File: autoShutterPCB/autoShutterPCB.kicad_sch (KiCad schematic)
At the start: 0 parts

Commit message: feat: Finish pcb, going to check how much it would cost
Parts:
- added Button1: SW_Push, Button_Switch_THT:SW_PUSH_6mm, symbol Switch:SW_Push
- added OLED1: Conn_01x04_Socket, Connector:FanPinHeader_1x04_P2.54mm_Vertical, symbol Connector:Conn_01x04_Socket
- added R1, R2, R3, R4: R, Resistor_THT:R_Axial_DIN0207_L6.3mm_D2.5mm_P10.16mm_Horizontal, symbol Device:R
- added TRS1: Conn_01x04_Socket, Audio_Module:TRS_SMD, symbol Connector:Conn_01x04_Socket
- added Transistor(Ring)1, Transistor(Tip)1: MMBT2222A, Package_TO_SOT_SMD:SOT-23, symbol Transistor_BJT:MMBT2222A
- added U1: XIAO-RP2040-DIP, Xiao RP2040:XIAO-RP2040-DIP, symbol Xiao RP2040:XIAO-RP2040-DIP
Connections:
- new net: R2.2, R3.1, Transistor(Ring)1.1 (B)
- new net: R1.2, R4.1, Transistor(Tip)1.1 (B)
- new net +3V3: OLED1.3 (Pin_3)
- new net GND: Button1.1, OLED1.4 (Pin_4), R3.2, R4.2, TRS1.2 (Pin_2), Transistor(Ring)1.2 (E), Transistor(Tip)1.2 (E), U1.13 (GND)
- new net d0: R1.1, U1.1 (P26_A0_D0)
- new net d1: R2.1, U1.2 (P27_A1_D1)
- new net d10B: Button1.2, U1.11 (P3_D10_MOSI)
- new net ring: TRS1.3 (Pin_3), Transistor(Ring)1.3 (C)
- new net scl: OLED1.1 (Pin_1), U1.6 (P7_SCL_D5)
- new net sda: OLED1.2 (Pin_2), U1.5 (P6_SDA_D4)
- new net tip: TRS1.4 (Pin_4), Transistor(Tip)1.3 (C)

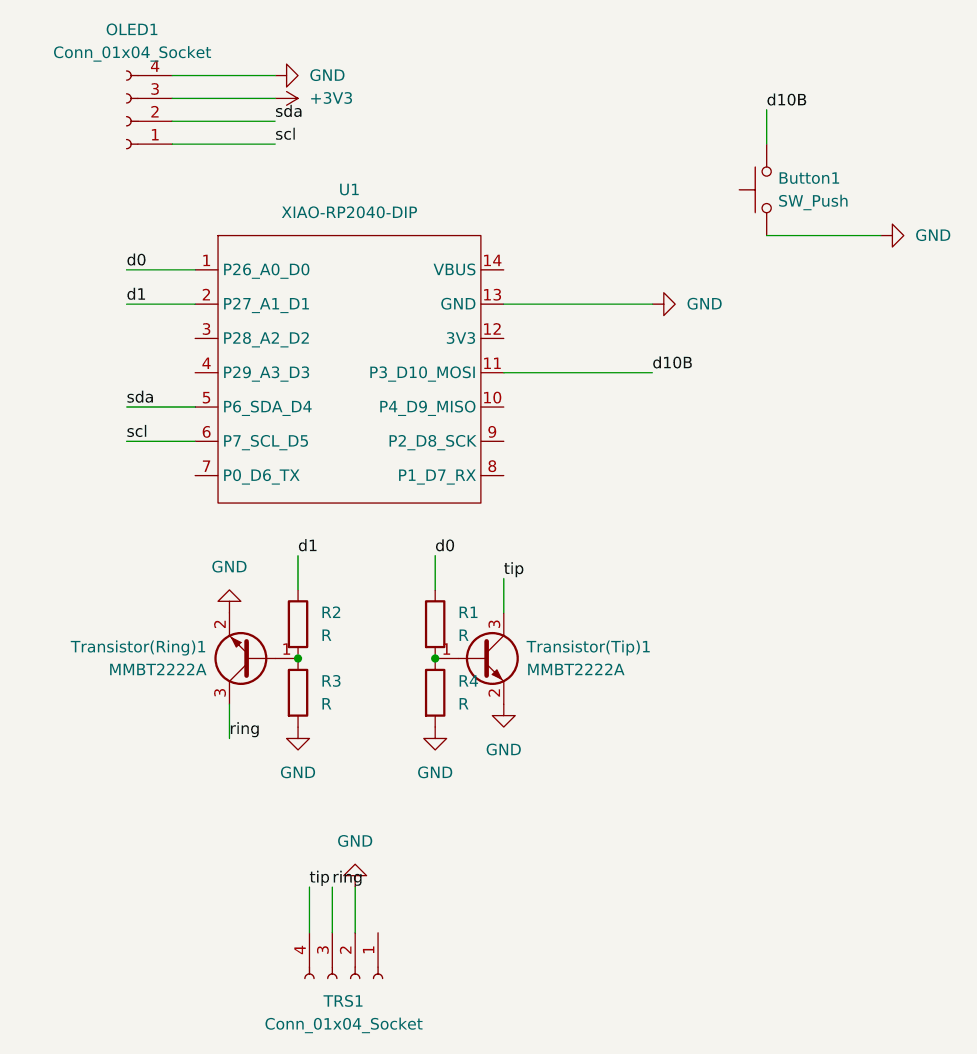
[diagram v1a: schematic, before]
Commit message: feat: Add digitalLevel dir
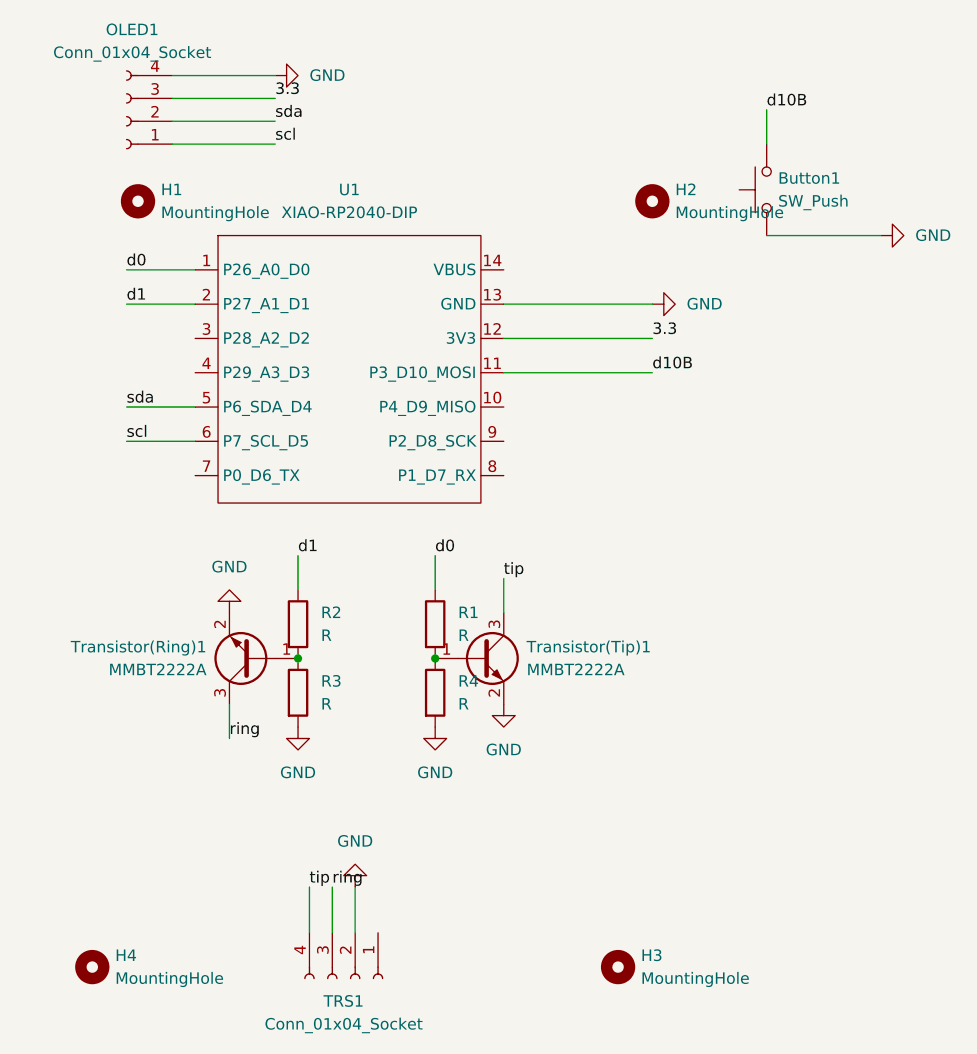
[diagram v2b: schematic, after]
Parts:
- added H1, H2, H3, H4: MountingHole, MountingHole:MountingHole_3.2mm_M3, symbol Mechanical:MountingHole
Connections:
- net +3V3 is gone; now on net 3.3: OLED1.3 (Pin_3)
- net 3.3: now reaches U1.12 (3V3)
